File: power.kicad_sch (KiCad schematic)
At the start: 58 parts, among them J4 Conn_02x02_Counter_Clockwise, Q3 Q_NMOS, Q4 Q_NMOS, Q5 Q_NMOS, Q6 Q_NMOS, U10 CJ431, U6 TPS5430DDA, U7 TPS56A37, U8 TPS2121, U9 LDL212PV33R

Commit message: pcb: run and fix DRC
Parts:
- U8: footprint Package_DFN_QFN:Texas_VQFN-HR-12_2x2.5mm_P0.5mm_ThermalVias -> Package_DFN_QFN:Texas_VQFN-HR-12_2x2.5mm_P0.5mm
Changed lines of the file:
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@@
 			)
 		)
-		(property "Footprint" "Package_DFN_QFN:Texas_VQFN-HR-12_2x2.5mm_P0.5mm_ThermalVias"
+		(property "Footprint" "Package_DFN_QFN:Texas_VQFN-HR-12_2x2.5mm_P0.5mm"
 			(at 161.29 126.492 0)
 			(effects

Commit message: schem: fix BOM
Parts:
- R37: JLCPCB Part # C20638 -> C17724; Manufacturer Part Number 0805W8F750JT5E -> 0805W8F510KT5E
- R38: JLCPCB Part # C23159 -> C25804; Manufacturer Part Number 0603WAF4301T5E -> 0603WAF1002T5E
- R39: JLCPCB Part # C22764 -> C23184; Manufacturer Part Number 0603WAF1101T5E -> 0603WAF4992T5E
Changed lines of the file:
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@@
 			)
 		)
-		(property "JLCPCB Part #" "C23159"
+		(property "JLCPCB Part #" "C25804"
 			(at 262.89 110.49 0)
 			(effects
@@
 			)
 		)
-		(property "Manufacturer Part Number" "0603WAF4301T5E"
+		(property "Manufacturer Part Number" "0603WAF1002T5E"
 			(at 262.89 110.49 0)
 			(effects
@@
 			)
 		)
-		(property "JLCPCB Part #" "C20638"
+		(property "JLCPCB Part #" "C17724"
 			(at 256.54 105.41 90)
 			(effects
@@
 			)
 		)
-		(property "Manufacturer Part Number" "0805W8F750JT5E"
+		(property "Manufacturer Part Number" "0805W8F510KT5E"
 			(at 256.54 105.41 90)
 			(effects
@@
 			)
 		)
-		(property "JLCPCB Part #" "C22764"
+		(property "JLCPCB Part #" "C23184"
 			(at 262.89 120.65 0)
 			(effects
@@
 			)
 		)
-		(property "Manufacturer Part Number" "0603WAF1101T5E"
+		(property "Manufacturer Part Number" "0603WAF4992T5E"
 			(at 262.89 120.65 0)
 			(effects

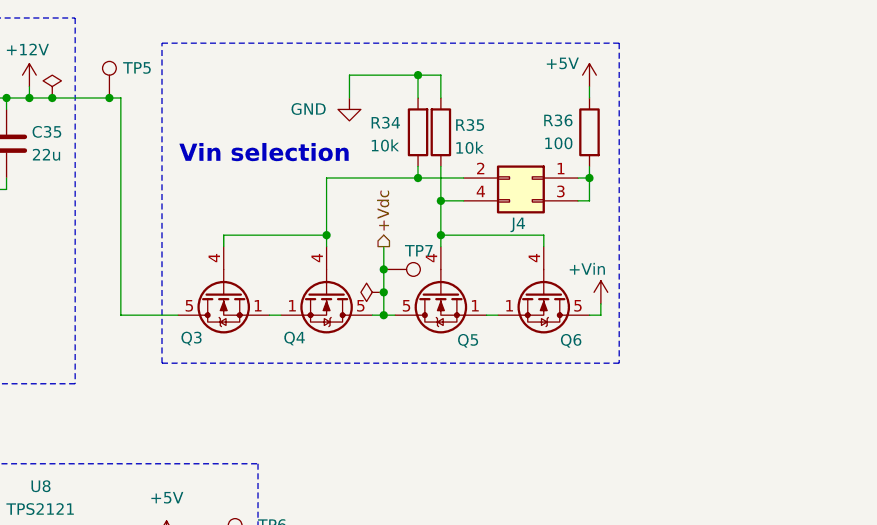
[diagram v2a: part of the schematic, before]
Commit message: schem: remove circular dependency for vin sel gate
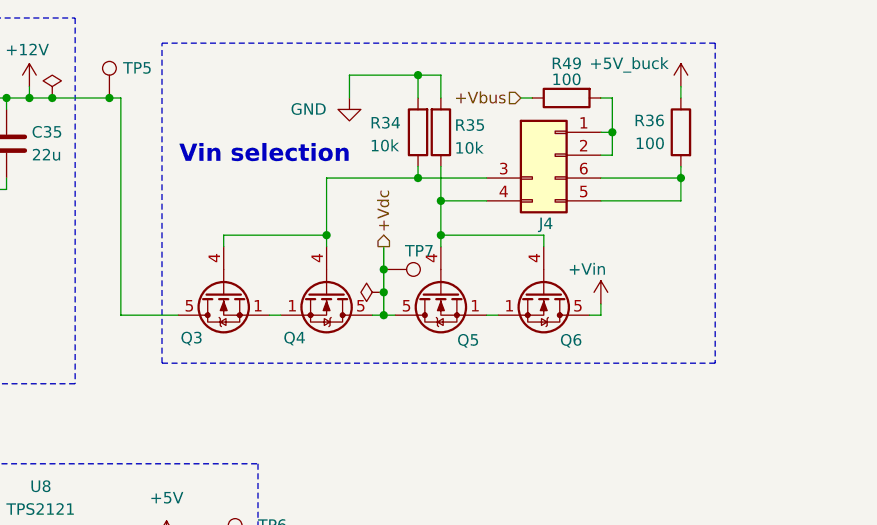
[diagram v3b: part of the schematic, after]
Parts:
- added R49: 100, Resistor_SMD:R_0603_1608Metric, symbol Device:R
- J4: footprint Connector_PinHeader_2.54mm:PinHeader_2x02_P2.54mm_Vertical -> Connector_PinHeader_2.54mm:PinHeader_2x03_P2.54mm_Vertical; symbol Connector_Generic:Conn_02x02_Odd_Even -> Connector_Generic:Conn_02x03_Odd_Even; now in the parts list
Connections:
- net +5V: no longer R36.1
- net +5V_buck: now also R36.1
- net +Vbus: now also R49.1
- net at Q3.4 (G), Q4.4 (G), R34.1: now also J4.3 (Pin_3); no longer J4.2 (Pin_2)
- new net: J4.5 (Pin_5), J4.6 (Pin_6), R36.2
- new net: J4.1 (Pin_1), J4.2 (Pin_2), R49.2
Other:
- moved on the sheet: R36

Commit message: schem: change antenna to available and add rf switch connector
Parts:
- J4: now left out of the parts list
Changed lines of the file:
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@@
 		(unit 1)
 		(exclude_from_sim no)
-		(in_bom yes)
+		(in_bom no)
 		(on_board yes)
 		(dnp no)
